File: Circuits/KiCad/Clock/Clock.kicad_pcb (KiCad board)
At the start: 2 copper layers, 38 parts, among them J1 Conn_01x05_Male, J2 Conn_01x02_Male, J3 Conn_01x02_Male, J4 Conn_01x02_Male, SW1 SW_Push, SW2 SW_Push_SPDT, SW3 SW_Push_SPDT, U1 74LS04, U2 NE555, U3 74LS08, U4 74LS32, U5 74LS08, U6 NE555, U7 NE555, U8 NE555, Y1 1 MHz

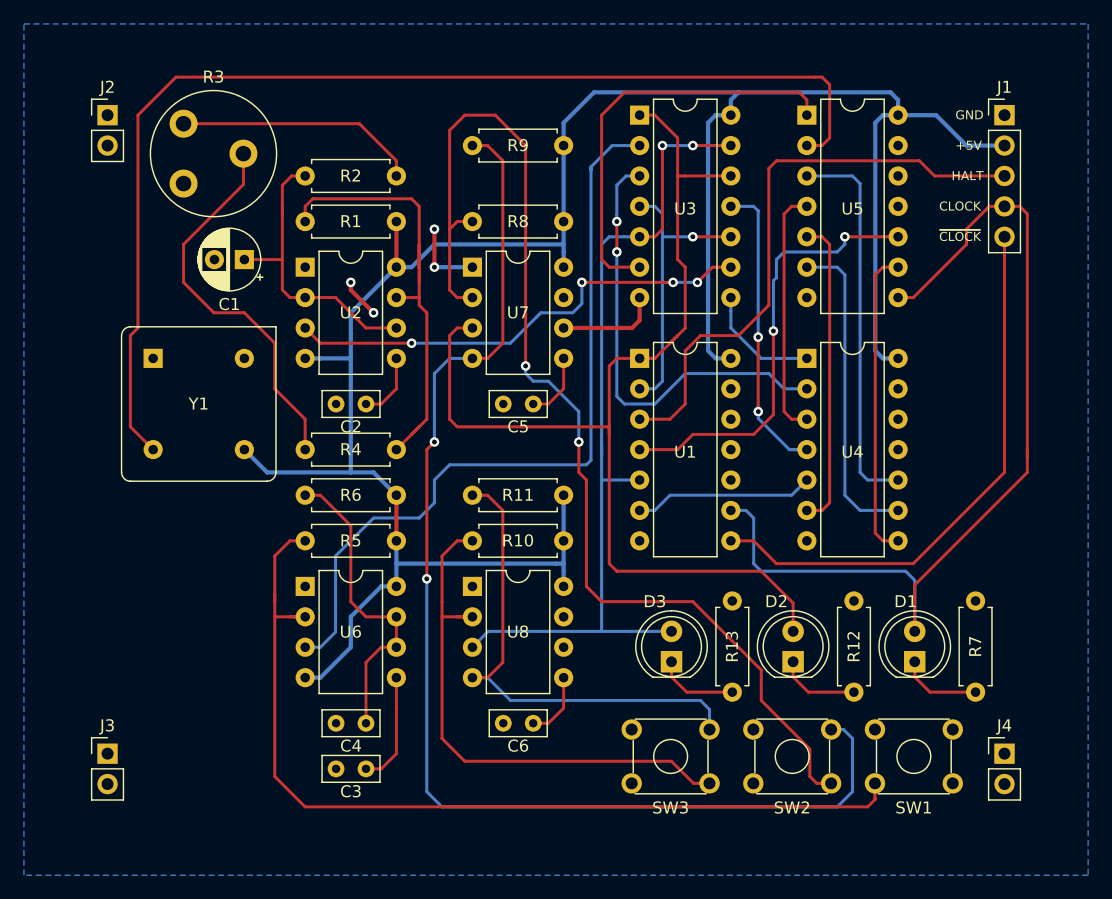
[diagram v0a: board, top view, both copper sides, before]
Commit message: Added Stack Pointer schematics & PCB. Rerouted Clock based autorouter output
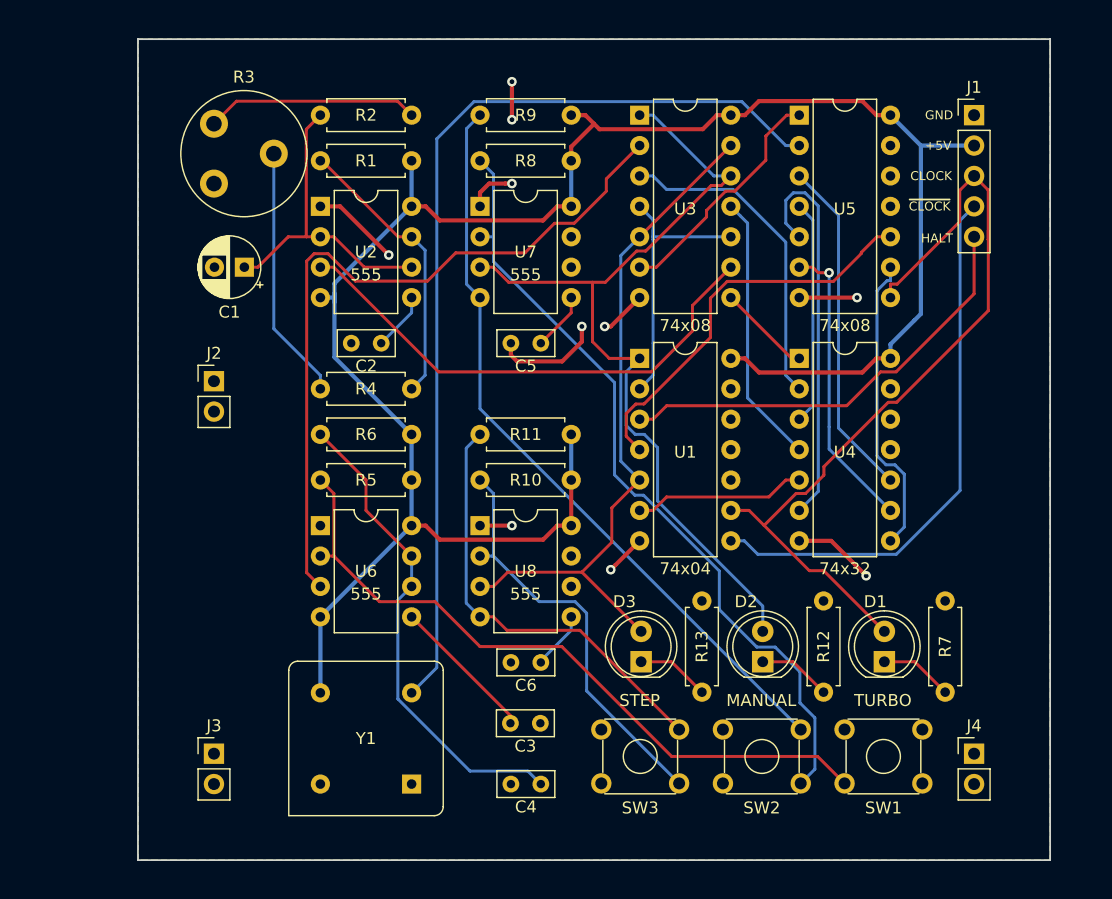
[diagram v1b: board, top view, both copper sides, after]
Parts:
- U1: value 74LS04 -> 74x04
- U2, U6, U7, U8: value NE555 -> 555
- U3, U5: value 74LS08 -> 74x08
- U4: value 74LS32 -> 74x32
- moved Y1 36.1 mm to (47.0, 80.0), turned to 0 degrees
- moved J2 23.9 mm to (38.1, 46.4)
- moved C4 15.5 mm to (65.4, 80.0)
- moved C3 12.7 mm to (62.9, 74.9), turned to 0 degrees
- moved J3 8.89 mm to (38.1, 77.5)
- moved R6 5.24 mm to (54.6, 50.8)
- moved R1 5.24 mm to (47.0, 27.9)
- moved R2 5.24 mm to (47.0, 24.1)
- moved C2 5.24 mm to (52.1, 43.2)
- moved R5 5.24 mm to (47.0, 54.6)
- moved U2 5.24 mm to (47.0, 31.8)
- moved U6 5.24 mm to (47.0, 58.4)
- moved R4 5.24 mm to (54.6, 47.0)
- moved C6 5.12 mm to (65.4, 69.8)
- moved R11 5.12 mm to (60.3, 50.8)
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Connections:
- J1 pad 3: CLK_HLT -> CLOCK
- J1 pad 4: CLOCK -> ~CLOCK
- J1 pad 5: ~CLOCK -> CLK_HLT
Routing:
- net Net-(R9-Pad1): track 103.4 -> 63.4 mm, vias 2 -> 0
- net +5V: track 198.3 -> 168.6 mm
- net Net-(R8-Pad1): track 95.4 -> 66.5 mm, vias 2 -> 0
- net GND: track 18.2 -> 45.4 mm, vias 4 -> 10
- net Net-(R5-Pad1): track 78.7 -> 58.5 mm
- net CLK_MAN_EN: track 92.1 -> 72.8 mm
- net Net-(R1-Pad1): track 40.8 -> 23.9 mm
- net Net-(U3-Pad6): track 35.0 -> 20.1 mm
- net CLK_TURBO: track 95.0 -> 80.2 mm
- net Net-(C4-Pad1): track 26.2 -> 40.6 mm
- net CLK_TURBO_EN: track 72.3 -> 58.1 mm, vias 2 -> 0
- net CLK_HLT: track 49.4 -> 37.0 mm
- net Net-(R3-Pad2): track 32.5 -> 21.3 mm
- net Net-(R10-Pad1): track 46.0 -> 35.1 mm
- net Net-(U3-Pad3): track 37.6 -> 27.2 mm, vias 2 -> 0
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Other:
- board outline added: 76.2 x 68.6 mm
- board text added: "MANUAL"
- board text added: "STEP"
- board text added: "TURBO"

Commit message: Updated a few Clock component footprints according to actual measurements
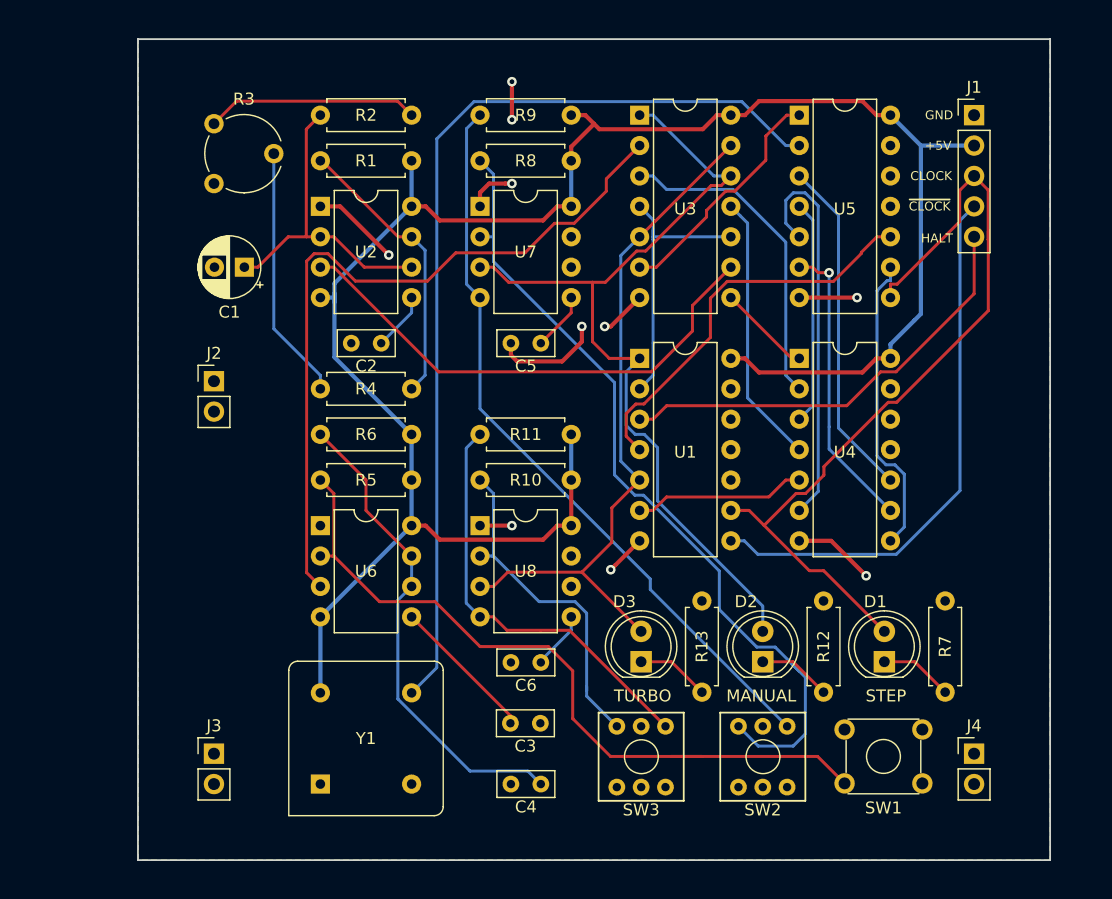
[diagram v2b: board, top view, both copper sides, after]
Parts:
- R3: footprint Potentiometer_THT:Potentiometer_Piher_PT-10-V05_Vertical -> Potentiometer_THT:Potentiometer_Piher_PT-6-V_Vertical
- SW2, SW3: footprint Button_Switch_THT:SW_TH_Tactile_Omron_B3F-10xx -> 74xx-Computer-Footprints:Switch
- moved SW2 3.88 mm to (83.9, 77.7)
- moved SW3 3.88 mm to (73.8, 77.7)
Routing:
- net Net-(R10-Pad1): track 35.1 -> 28.5 mm
- net Net-(R5-Pad1): track 58.5 -> 63.3 mm
- net Net-(R8-Pad1): track 66.5 -> 69.2 mm
- net Net-(R11-Pad1): track 36.7 -> 35.5 mm
- net Net-(R9-Pad1): track 63.4 -> 62.6 mm

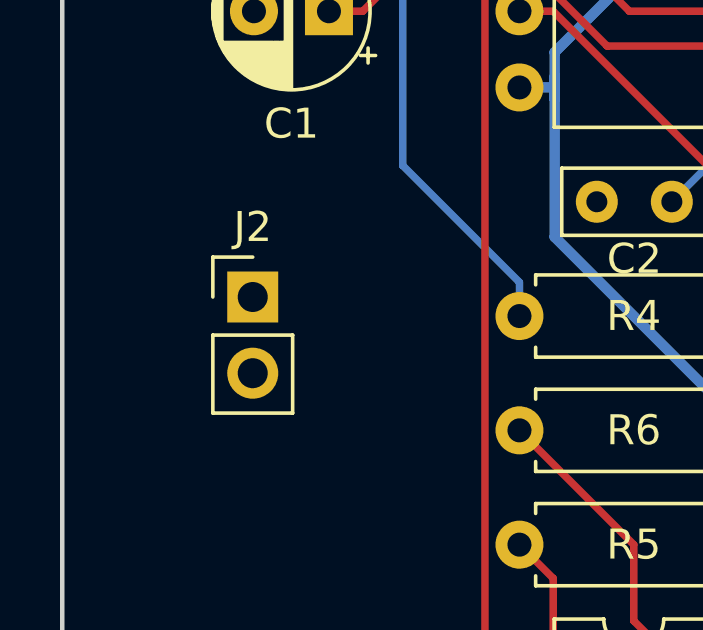
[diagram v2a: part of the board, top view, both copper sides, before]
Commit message: Made sure spacing between headers is always 2.54mm pitch
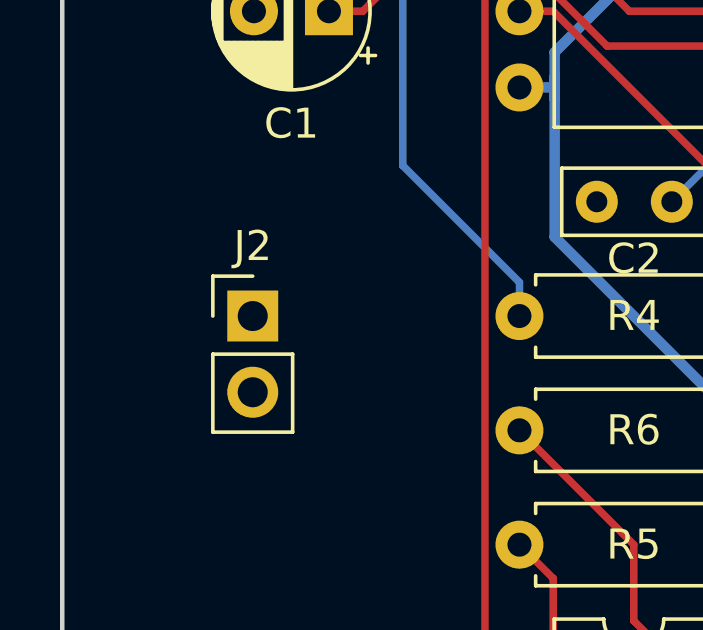
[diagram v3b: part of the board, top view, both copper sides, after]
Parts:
- moved J2 0.64 mm to (38.1, 47.0)
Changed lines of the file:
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@@
   )
   (module Connector_PinHeader_2.54mm:PinHeader_1x02_P2.54mm_Vertical (layer F.Cu)
-    (at 38.1 46.355)
+    (at 38.1 46.99)
     (descr "Through hole straight pin header, 1x02, 2.54mm pitch, single row")
     (tags "Through hole pin header THT 1x02 2.54mm single row")

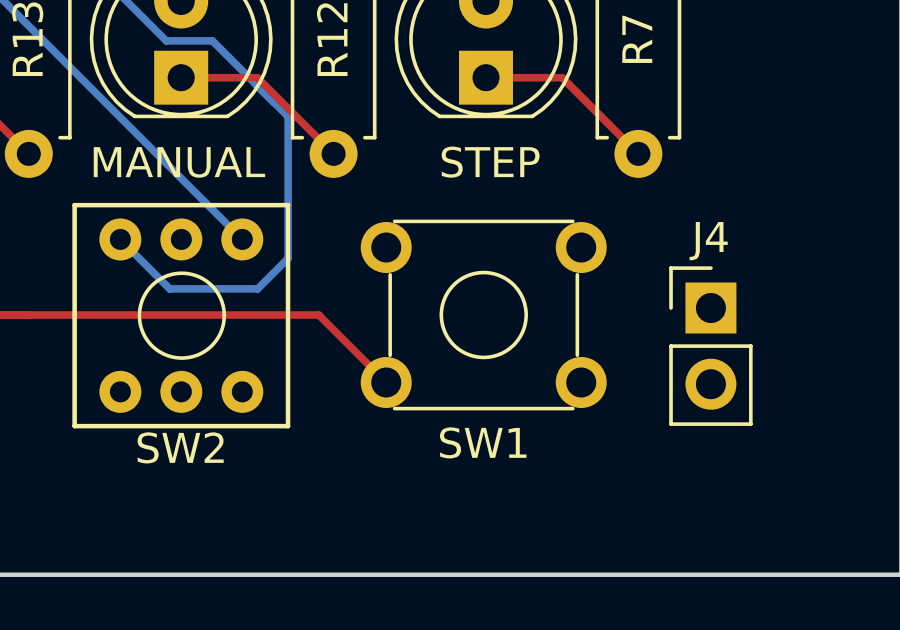
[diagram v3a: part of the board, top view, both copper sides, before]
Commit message: Built Clock circuit on PCB and updated design accordingly. Added footprint for a few exotic components
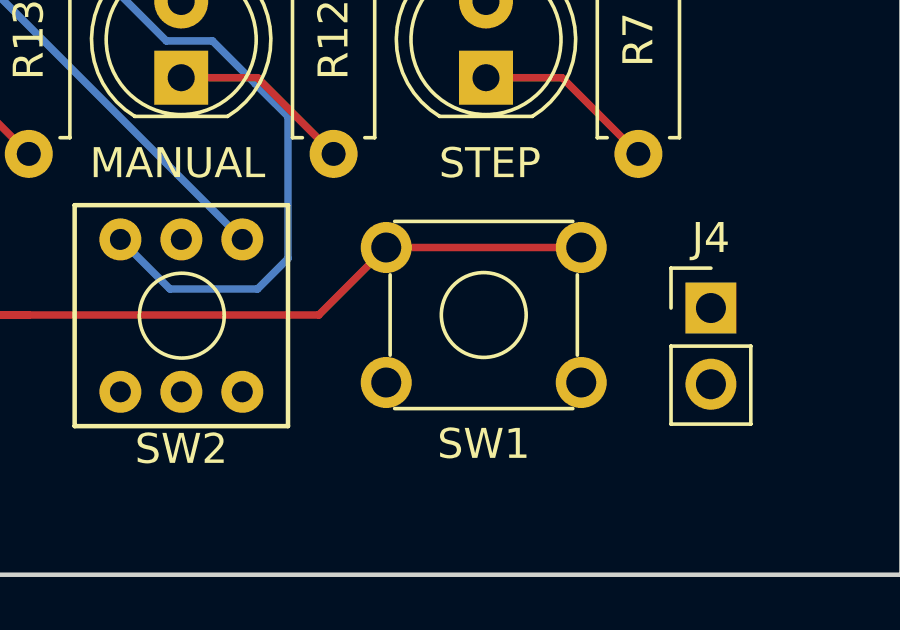
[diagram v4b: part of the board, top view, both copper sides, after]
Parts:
- SW1: footprint Button_Switch_THT:SW_TH_Tactile_Omron_B3F-10xx -> 74xx-Computer-Footprints:SW_6mm_Tact
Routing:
- net Net-(R5-Pad1): track 63.3 -> 69.8 mm
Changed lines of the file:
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@@
     (thickness 1.6)
     (drawings 16)
-    (tracks 354)
+    (tracks 355)
     (zones 0)
     (modules 38)
@@
     (add_net GND)
   )
+  (module 74xx-Computer-Footprints:SW_6mm_Tact (layer F.Cu)
+    (at 97.2774 79.9524 180)
+    (descr SW_TH_Tactile_Omron_B3F-10xx_https://www.omron.com/ecb/products/pdf/en-b3f.pdf)
+    (tags "Omron B3F-10xx")
+    (fp_text reference SW1 (at 3.25 -2.05 180) (layer F.SilkS)
+      (effects (font (size 1 1) (thickness 0.15)))
+    )
+    (fp_text value SW_Push (at 3.2 6.5 180) (layer F.Fab)
+      (effects (font (size 1 1) (thickness 0.15)))
+    )
+    (fp_line (start 0.25 5.25) (end 6.25 5.25) (layer F.Fab) (width 0.1))
+    (fp_line (start 6.37 0.91) (end 6.37 3.59) (layer F.SilkS) (width 0.12))
+    (fp_line (start 0.13 3.59) (end 0.13 0.91) (layer F.SilkS) (width 0.12))
+    (fp_line (start 0.28 -0.87) (end 6.22 -0.87) (layer F.SilkS) (width 0.12))
+    (fp_line (start 0.28 5.37) (end 6.22 5.37) (layer F.SilkS) (width 0.12))
+    (fp_circle (center 3.25 2.25) (end 4.25 3.25) (layer F.SilkS) (width 0.12))
+    (fp_line (start -1.1 -1.15) (end -1.1 5.6) (layer F.CrtYd) (width 0.05))
+    (fp_line (start -1.1 5.6) (end 7.6 5.6) (layer F.CrtYd) (width 0.05))
+    (fp_line (start 7.6 5.6) (end 7.6 -1.1) (layer F.CrtYd) (width 0.05))
+    (fp_line (start 7.65 -1.15) (end -1.1 -1.15) (layer F.CrtYd) (width 0.05))
+    (fp_text user %R (at 3.25 2.25 180) (layer F.Fab)
+      (effects (font (size 1 1) (thickness 0.15)))
+    )
+    (fp_line (start 0.25 -0.75) (end 6.25 -0.75) (layer F.Fab) (width 0.1))
+    (fp_line (start 6.25 -0.75) (end 6.25 5.25) (layer F.Fab) (width 0.1))
+    (fp_line (start 0.25 -0.75) (end 0.25 5.25) (layer F.Fab) (width 0.1))
+    (pad 1 thru_hole circle (at 0 0 180) (size 1.7 1.7) (drill 1) (layers *.Cu *.Mask)
+      (net 2 GND))
+    (pad 1 thru_hole circle (at 6.5 0 180) (size 1.7 1.7) (drill 1) (layers *.Cu *.Mask)
+      (net 2 GND))
+    (pad 2 thru_hole circle (at 0 4.5 180) (size 1.7 1.7) (drill 1) (layers *.Cu *.Mask)
+      (net 40 "Net-(R5-Pad1)"))
+    (pad 2 thru_hole circle (at 6.5 4.5 180) (size 1.7 1.7) (drill 1) (layers *.Cu *.Mask)
+      (net 40 "Net-(R5-Pad1)"))
+    (model ${KISYS3DMOD}/Button_Switch_THT.3dshapes/SW_TH_Tactile_Omron_B3F-10xx.wrl
+      (at (xyz 0 0 0))
+      (scale (xyz 1 1 1))
+      (rotate (xyz 0 0 0))
+    )
+  )
   (module 74xx-Computer-Footprints:Switch (layer F.Cu)
     (at 83.947 77.724 180)
@@
     (pad 4 thru_hole rect (at 0 0) (size 1.6 1.6) (drill 0.8) (layers *.Cu *.Mask))
     (model ${KISYS3DMOD}/Oscillator.3dshapes/Oscillator_DIP-8.wrl
-      (at (xyz 0 0 0))
-      (scale (xyz 1 1 1))
-      (rotate (xyz 0 0 0))
-    )
-  )
-  (module Button_Switch_THT:SW_TH_Tactile_Omron_B3F-10xx (layer F.Cu)
-    (at 97.2774 79.9524 180)
-    (descr SW_TH_Tactile_Omron_B3F-10xx_https://www.omron.com/ecb/products/pdf/en-b3f.pdf)
-    (tags "Omron B3F-10xx")
-    (fp_text reference SW1 (at 3.25 -2.05 180) (layer F.SilkS)
-      (effects (font (size 1 1) (thickness 0.15)))
-    )
-    (fp_text value SW_Push (at 3.2 6.5 180) (layer F.Fab)
-      (effects (font (size 1 1) (thickness 0.15)))
-    )
-    (fp_line (start 0.25 5.25) (end 6.25 5.25) (layer F.Fab) (width 0.1))
-    (fp_line (start 6.37 0.91) (end 6.37 3.59) (layer F.SilkS) (width 0.12))
-    (fp_line (start 0.13 3.59) (end 0.13 0.91) (layer F.SilkS) (width 0.12))
-    (fp_line (start 0.28 -0.87) (end 6.22 -0.87) (layer F.SilkS) (width 0.12))
-    (fp_line (start 0.28 5.37) (end 6.22 5.37) (layer F.SilkS) (width 0.12))
-    (fp_circle (center 3.25 2.25) (end 4.25 3.25) (layer F.SilkS) (width 0.12))
-    (fp_line (start -1.1 -1.15) (end -1.1 5.6) (layer F.CrtYd) (width 0.05))
-    (fp_line (start -1.1 5.6) (end 7.6 5.6) (layer F.CrtYd) (width 0.05))
-    (fp_line (start 7.6 5.6) (end 7.6 -1.1) (layer F.CrtYd) (width 0.05))
-    (fp_line (start 7.65 -1.15) (end -1.1 -1.15) (layer F.CrtYd) (width 0.05))
-    (fp_text user %R (at 3.25 2.25 180) (layer F.Fab)
-      (effects (font (size 1 1) (thickness 0.15)))
-    )
-    (fp_line (start 0.25 -0.75) (end 6.25 -0.75) (layer F.Fab) (width 0.1))
-    (fp_line (start 6.25 -0.75) (end 6.25 5.25) (layer F.Fab) (width 0.1))
-    (fp_line (start 0.25 -0.75) (end 0.25 5.25) (layer F.Fab) (width 0.1))
-    (pad 1 thru_hole circle (at 0 0 180) (size 1.7 1.7) (drill 1) (layers *.Cu *.Mask)
-      (net 2 GND))
-    (pad 2 thru_hole circle (at 6.5 0 180) (size 1.7 1.7) (drill 1) (layers *.Cu *.Mask)
-      (net 40 "Net-(R5-Pad1)"))
-    (pad 3 thru_hole circle (at 0 4.5 180) (size 1.7 1.7) (drill 1) (layers *.Cu *.Mask))
-    (pad 4 thru_hole circle (at 6.5 4.5 180) (size 1.7 1.7) (drill 1) (layers *.Cu *.Mask))
-    (model ${KISYS3DMOD}/Button_Switch_THT.3dshapes/SW_TH_Tactile_Omron_B3F-10xx.wrl
       (at (xyz 0 0 0))
       (scale (xyz 1 1 1))
@@
   (segment (start 51.9253 64.77) (end 56.5698 64.77) (width 0.25) (layer F.Cu) (net 40))
   (segment (start 56.5698 64.77) (end 60.3243 68.5245) (width 0.25) (layer F.Cu) (net 40))
-  (segment (start 88.5274 77.7024) (end 90.7774 79.9524) (width 0.25) (layer F.Cu) (net 40))
   (segment (start 48.1153 60.96) (end 48.1153 55.7353) (width 0.25) (layer F.Cu) (net 40))
   (segment (start 48.1153 55.7353) (end 46.99 54.61) (width 0.25) (layer F.Cu) (net 40))
@@
   (segment (start 76.3374 77.7024) (end 78.867 77.7024) (width 0.25) (layer F.Cu) (net 40))
   (segment (start 78.867 77.7024) (end 88.5274 77.7024) (width 0.25) (layer F.Cu) (net 40))
+  (segment (start 88.5274 77.7024) (end 90.7774 75.4524) (width 0.25) (layer F.Cu) (net 40))
+  (segment (start 90.7774 75.4524) (end 97.2774 75.4524) (width 0.25) (layer F.Cu) (net 40))
   (segment (start 61.4503 34.29) (end 61.4503 29.0653) (width 0.25) (layer B.Cu) (net 41))
   (segment (start 61.4503 29.0653) (end 60.325 27.94) (width 0.25) (layer B.Cu) (net 41))
